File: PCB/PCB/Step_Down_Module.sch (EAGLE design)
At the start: 22 parts, among them Q1 TPH2900ENH

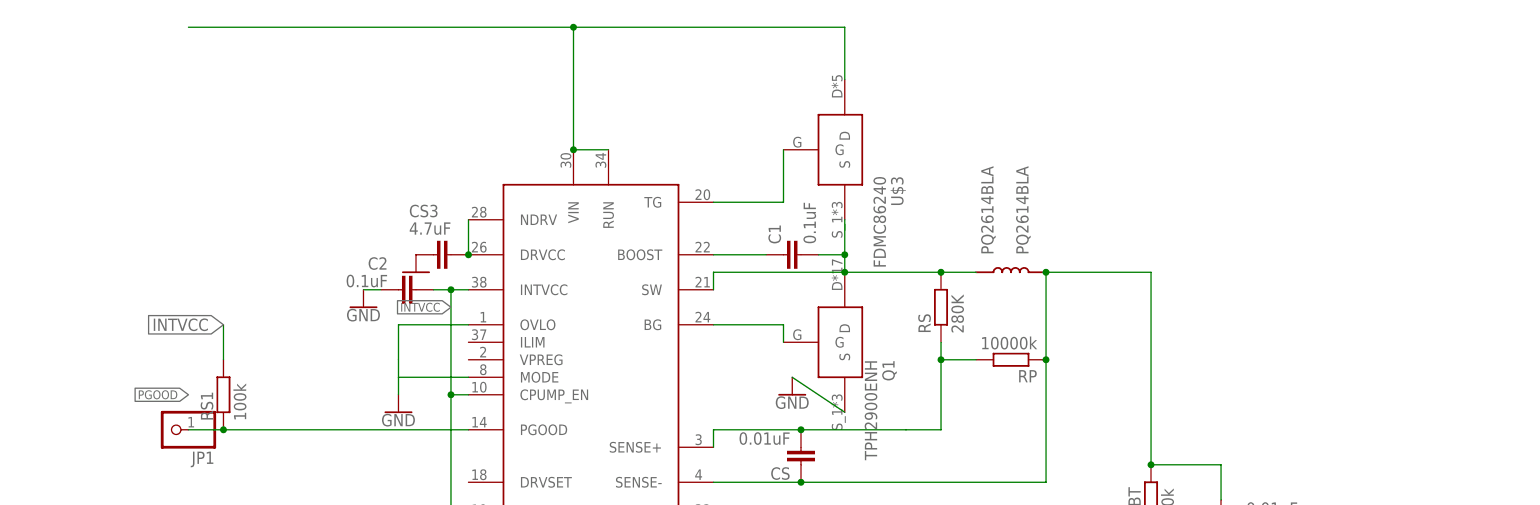
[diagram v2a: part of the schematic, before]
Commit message: Working on schematic - Added I/O capacitors
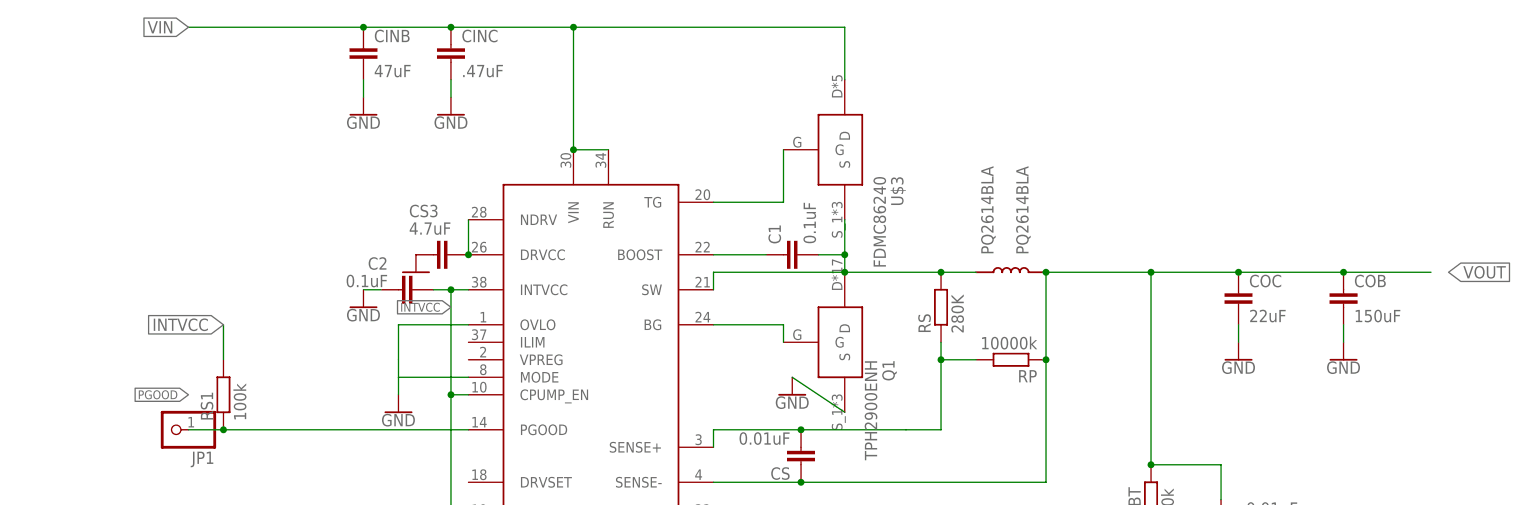
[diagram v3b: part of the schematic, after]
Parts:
- added CINB: 47uF, rcl:C-EUC0805
- added CINC: .47uF, rcl:C-EUC0805
- added COB: 150uF, rcl:C-EUC0805
- added COC: 22uF, rcl:C-EUC0805
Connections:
- removed net N$5: CS.1, CS1.2, RFBT.2, RP.1, U$1.SENSE-, U$2.P$2
- removed net N$9: U$1.RUN, U$1.VIN, U$3.D
- new net VIN: CINB.1, CINC.1, U$1.RUN, U$1.VIN, U$3.D
- new net VOUT: COB.1, COC.1, CS.1, CS1.2, RFBT.2, RP.1, U$1.SENSE-, U$2.P$2
- net GND: now also CINB.2, CINC.2, COB.2, COC.2
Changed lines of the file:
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@@
 <part name="CS3" library="rcl" library_urn="urn:adsk.eagle:library:334" deviceset="C-EU" device="C0805" package3d_urn="urn:adsk.eagle:package:23617/2" value="4.7uF"/>
 <part name="GND10" library="SparkFun-PowerSymbols" library_urn="urn:adsk.eagle:library:530" deviceset="GND" device=""/>
+<part name="CINB" library="rcl" library_urn="urn:adsk.eagle:library:334" deviceset="C-EU" device="C0805" package3d_urn="urn:adsk.eagle:package:23617/2" value="47uF"/>
+<part name="CINC" library="rcl" library_urn="urn:adsk.eagle:library:334" deviceset="C-EU" device="C0805" package3d_urn="urn:adsk.eagle:package:23617/2" value=".47uF"/>
+<part name="COC" library="rcl" library_urn="urn:adsk.eagle:library:334" deviceset="C-EU" device="C0805" package3d_urn="urn:adsk.eagle:package:23617/2" value="22uF"/>
+<part name="COB" library="rcl" library_urn="urn:adsk.eagle:library:334" deviceset="C-EU" device="C0805" package3d_urn="urn:adsk.eagle:package:23617/2" value="150uF"/>
+<part name="GND11" library="SparkFun-PowerSymbols" library_urn="urn:adsk.eagle:library:530" deviceset="GND" device=""/>
+<part name="GND12" library="SparkFun-PowerSymbols" library_urn="urn:adsk.eagle:library:530" deviceset="GND" device=""/>
+<part name="GND13" library="SparkFun-PowerSymbols" library_urn="urn:adsk.eagle:library:530" deviceset="GND" device=""/>
+<part name="GND14" library="SparkFun-PowerSymbols" library_urn="urn:adsk.eagle:library:530" deviceset="GND" device=""/>
 </parts>
 <sheets>
@@
 </instance>
 <instance part="GND10" gate="1" x="-5.08" y="73.66" smashed="yes"/>
+<instance part="CINB" gate="G$1" x="-12.7" y="106.68"/>
+<instance part="CINC" gate="G$1" x="0" y="106.68"/>
+<instance part="COC" gate="G$1" x="114.3" y="71.12"/>
+<instance part="COB" gate="G$1" x="129.54" y="71.12"/>
+<instance part="GND11" gate="1" x="114.3" y="60.96"/>
+<instance part="GND12" gate="1" x="129.54" y="60.96"/>
+<instance part="GND13" gate="1" x="-12.7" y="96.52"/>
+<instance part="GND14" gate="1" x="0" y="96.52"/>
 </instances>
 <busses>
@@
 </segment>
 </net>
-<net name="N$5" class="0">
+<net name="VOUT" class="0">
 <segment>
 <pinref part="U$2" gate="G$1" pin="P$2"/>
@@
 <wire x1="111.76" y1="45.72" x2="111.76" y2="40.64" width="0.1524" layer="91"/>
 <junction x="101.6" y="45.72"/>
+<pinref part="COC" gate="G$1" pin="1"/>
+<wire x1="114.3" y1="73.66" x2="101.6" y2="73.66" width="0.1524" layer="91"/>
+<junction x="101.6" y="73.66"/>
+<pinref part="COB" gate="G$1" pin="1"/>
+<wire x1="129.54" y1="73.66" x2="114.3" y2="73.66" width="0.1524" layer="91"/>
+<junction x="114.3" y="73.66"/>
+<wire x1="129.54" y1="73.66" x2="142.24" y2="73.66" width="0.1524" layer="91"/>
+<junction x="129.54" y="73.66"/>
+<label x="144.78" y="73.66" size="1.778" layer="95" xref="yes"/>
 </segment>
 </net>
@@
 </segment>
 </net>
-<net name="N$9" class="0">
+<net name="VIN" class="0">
 <segment>
 <pinref part="U$1" gate="G$1" pin="VIN"/>
@@
 <wire x1="17.78" y1="91.44" x2="22.86" y2="91.44" width="0.1524" layer="91"/>
 <wire x1="17.78" y1="91.44" x2="17.78" y2="109.22" width="0.1524" layer="91"/>
-<wire x1="17.78" y1="109.22" x2="-38.1" y2="109.22" width="0.1524" layer="91"/>
+<wire x1="17.78" y1="109.22" x2="0" y2="109.22" width="0.1524" layer="91"/>
 <junction x="17.78" y="91.44"/>
 <pinref part="U$3" gate="G$1" pin="D"/>
+<wire x1="0" y1="109.22" x2="-12.7" y2="109.22" width="0.1524" layer="91"/>
+<wire x1="-12.7" y1="109.22" x2="-38.1" y2="109.22" width="0.1524" layer="91"/>
 <wire x1="57.15" y1="101.6" x2="57.15" y2="109.22" width="0.1524" layer="91"/>
 <wire x1="57.15" y1="109.22" x2="17.78" y2="109.22" width="0.1524" layer="91"/>
 <junction x="17.78" y="109.22"/>
+<pinref part="CINB" gate="G$1" pin="1"/>
+<junction x="-12.7" y="109.22"/>
+<pinref part="CINC" gate="G$1" pin="1"/>
+<junction x="0" y="109.22"/>
+<label x="-38.1" y="109.22" size="1.778" layer="95" rot="R180" xref="yes"/>
 </segment>
 </net>
@@
 <pinref part="GND10" gate="1" pin="GND"/>
 </segment>
-</net>
+<segment>
+<pinref part="GND13" gate="1" pin="GND"/>
+<pinref part="CINB" gate="G$1" pin="2"/>
+<wire x1="-12.7" y1="99.06" x2="-12.7" y2="101.6" width="0.1524" layer="91"/>
+</segment>
+<segment>
+<pinref part="GND14" gate="1" pin="GND"/>
+<pinref part="CINC" gate="G$1" pin="2"/>
+<wire x1="0" y1="99.06" x2="0" y2="101.6" width="0.1524" layer="91"/>
+</segment>
+<segment>
+<pinref part="GND11" gate="1" pin="GND"/>
+<pinref part="COC" gate="G$1" pin="2"/>
+<wire x1="114.3" y1="63.5" x2="114.3" y2="66.04" width="0.1524" layer="91"/>
+</segment>
+<segment>
+<pinref part="GND12" gate="1" pin="GND"/>
+<pinref part="COB" gate="G$1" pin="2"/>
+<wire x1="129.54" y1="63.5" x2="129.54" y2="66.04" width="0.1524" layer="91"/>
+</segment>
+</net>

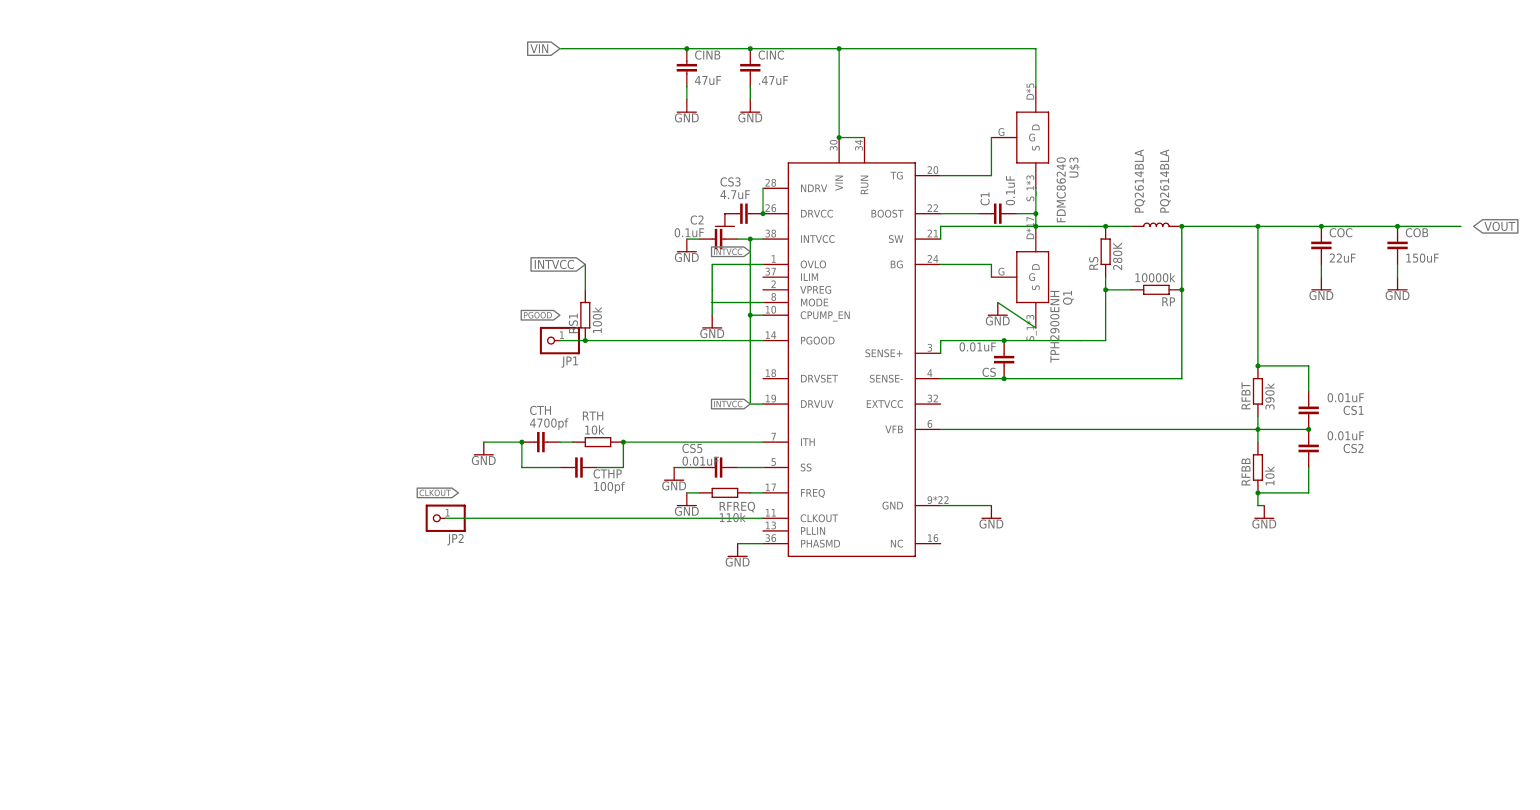
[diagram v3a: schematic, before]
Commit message: Working on schematic - Added DRVCC transistor, made a lot of changes to the pin state
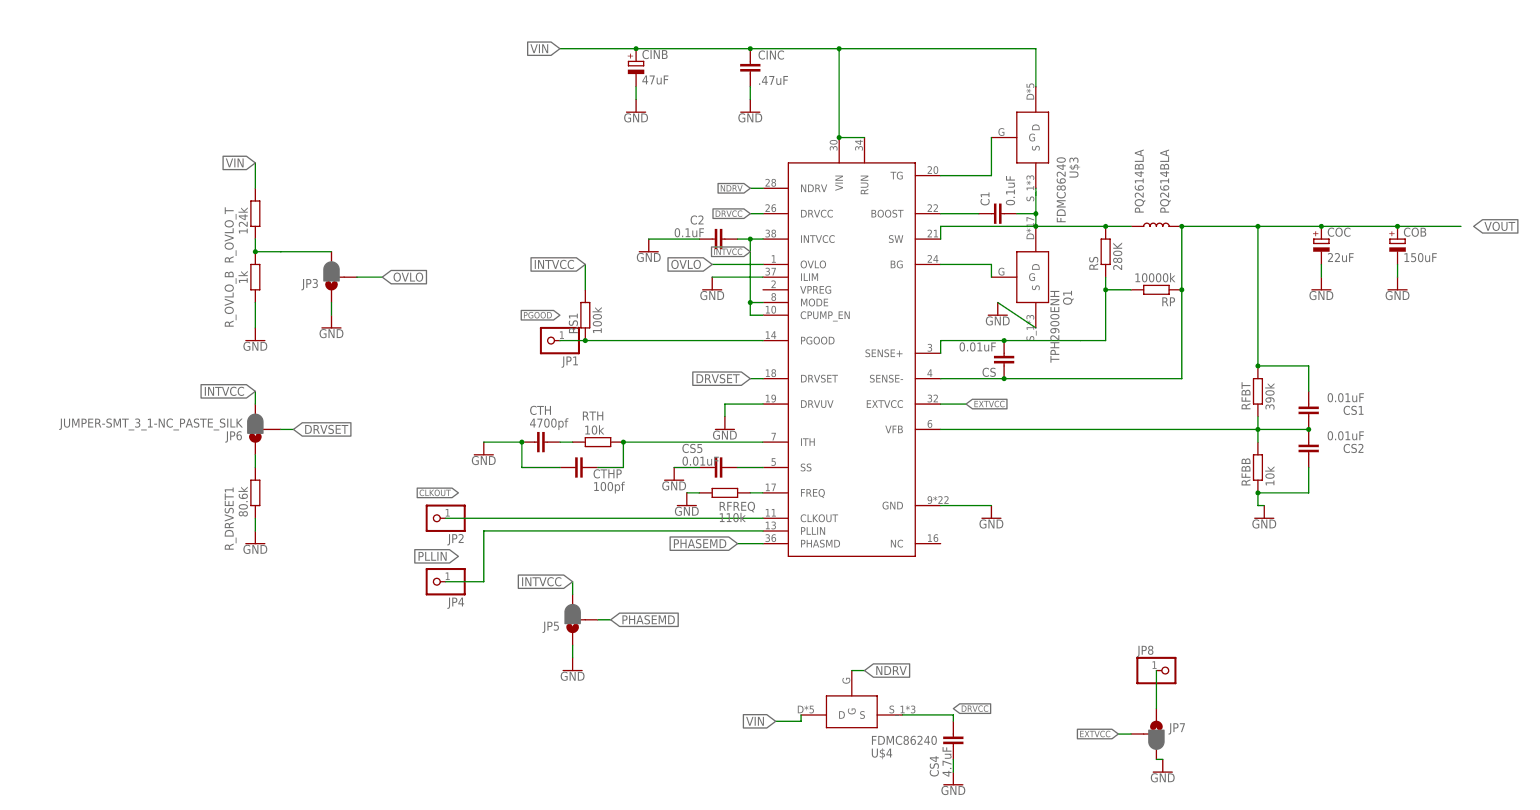
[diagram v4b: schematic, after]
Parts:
- removed CS3: 4.7uF, rcl:C-EUC0805
- added CS4: 4.7uF, rcl:C-EUC0805
- added JP3, JP5, JP6, JP7: JUMPER-SMT_3_1-NC_PASTE_SILK, SparkFun-Jumpers:JUMPER-SMT_3_1-NC_PASTE_SILK
- added JP4, JP8: (no value), pinhead:PINHD-1X1
- added R_DRVSET1: 80.6k, rcl:R-EU_R0805
- added R_OVLO_B: 1k, rcl:R-EU_R0805
- added R_OVLO_T: 124k, rcl:R-EU_R0805
- added U$4: FDMC86240, Switching_MOS:FDMC86240
- CINB: device rcl:C-EUC0805 -> rcl:CPOL-EUE7.5-16
- CINC: device rcl:C-EUC0805 -> rcl:C-EU150-084X183
- COB: device rcl:C-EUC0805 -> rcl:CPOL-EUE5-10.5
- COC: device rcl:C-EUC0805 -> rcl:CPOL-EUE5-5
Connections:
- removed net N$14: CS3.1, U$1.DRVCC, U$1.NDRV
- new net DRVCC: CS4.1, U$1.DRVCC, U$4.S
- new net DRVSET: JP6.2, U$1.DRVSET
- new net EXTVCC: JP7.2, U$1.EXTVCC
- new net N$13: JP7.1, JP8.1
- new net N$5: JP6.1, R_DRVSET1.1
- new net N$9: JP3.3, R_OVLO_B.1, R_OVLO_T.2
- new net NDRV: U$1.NDRV, U$4.G
- new net OVLO: JP3.2, U$1.OVLO
- new net PHASEMD: JP5.2, U$1.PHASMD
- new net PLLIN: JP4.1, U$1.PLLIN
- net GND: now also CINB.-, COB.-, COC.-, CS4.2, JP3.1, JP5.1, JP7.3, R_DRVSET1.2, R_OVLO_B.2, U$1.DRVUV, U$1.ILIM; no longer CINB.2, COB.2, COC.2, CS3.2, U$1.MODE, U$1.OVLO, U$1.PHASMD
- net INTVCC: now also JP5.3, JP6.3, U$1.MODE; no longer U$1.DRVUV
- net VIN: now also CINB.+, R_OVLO_T.1, U$4.D; no longer CINB.1
- net VOUT: now also COB.+, COC.+; no longer COB.1, COC.1

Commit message: Removed folder: Adithya
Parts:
- removed C1: 0.1uF, rcl:C-EUC0805
- added CINC1: .47uF, rcl:C-EU150-084X183
- added COB1: 150uF, rcl:CPOL-EUE5-10.5
- added COC1: 22uF, rcl:CPOL-EUE5-5
- added POT_FB: 10k, rcl:R-TRIMM64W
- added RS2: 10k, rcl:R-EU_R0805
- RFBB: value 10k -> 4.7k
- RFBT: value 390k -> 180k
- RS: value 280K -> 270k
- R_OVLO_T: value 124k -> 120k
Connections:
- net N$10 renamed ITH
- net N$7 renamed SS
- new net N$14: CS1.2, POT_FB.S, RFBT.2
- new net N$7: RS.1, RS2.2
- net GND: now also COB1.-, COC1.-, POT_FB.E
- net N$3: now also CINC1.2; no longer C1.2
- net N$4: now also CINC1.1; no longer C1.1
- net N$6: now also RS2.1; no longer RS.1
- net VOUT: now also COB1.+, COC1.+, POT_FB.A; no longer CS1.2, RFBT.2
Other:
- moved on the sheet: RP

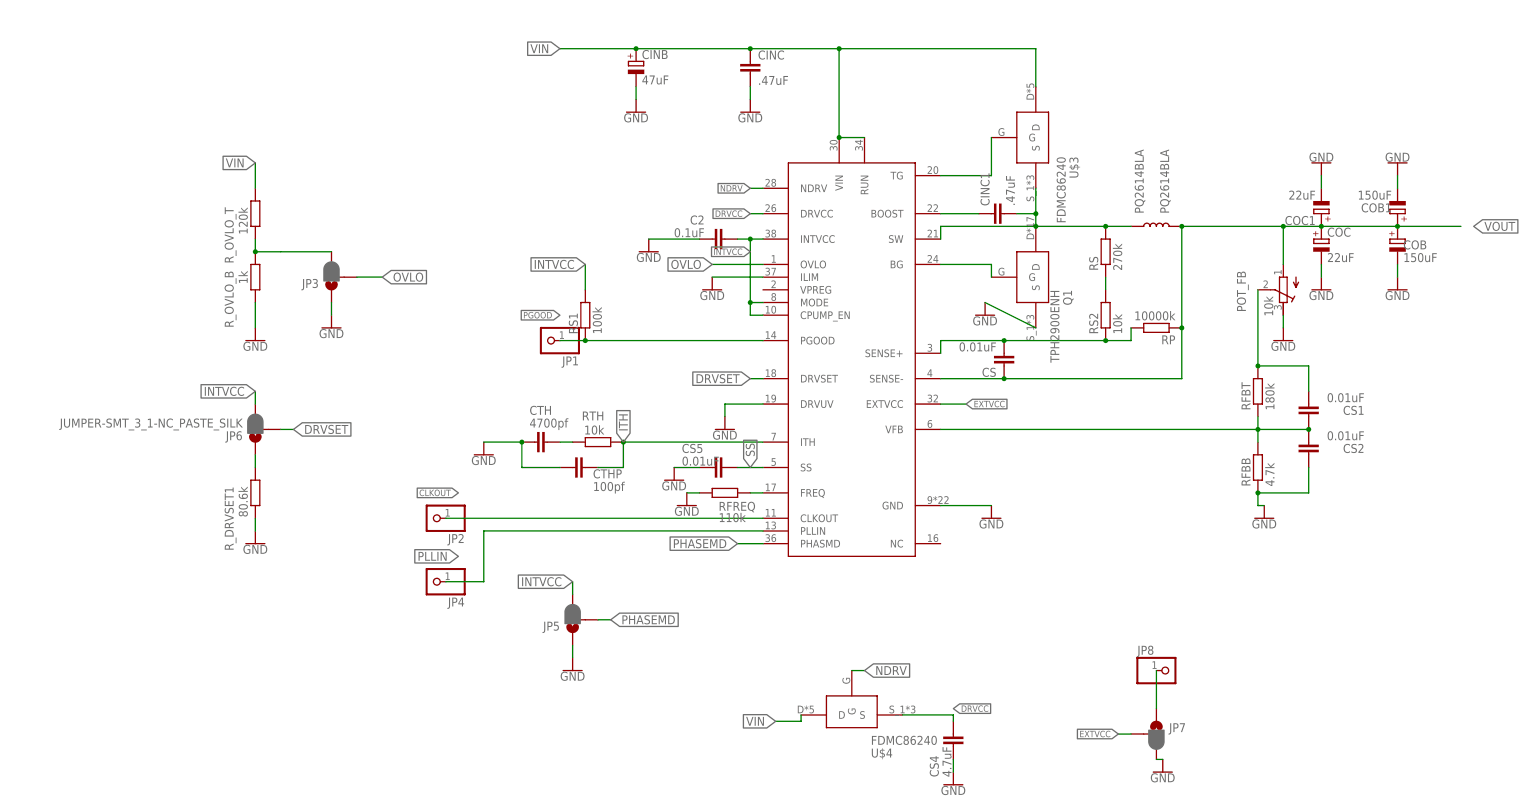
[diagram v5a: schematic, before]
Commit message: Initial routing of PCB with design considerations
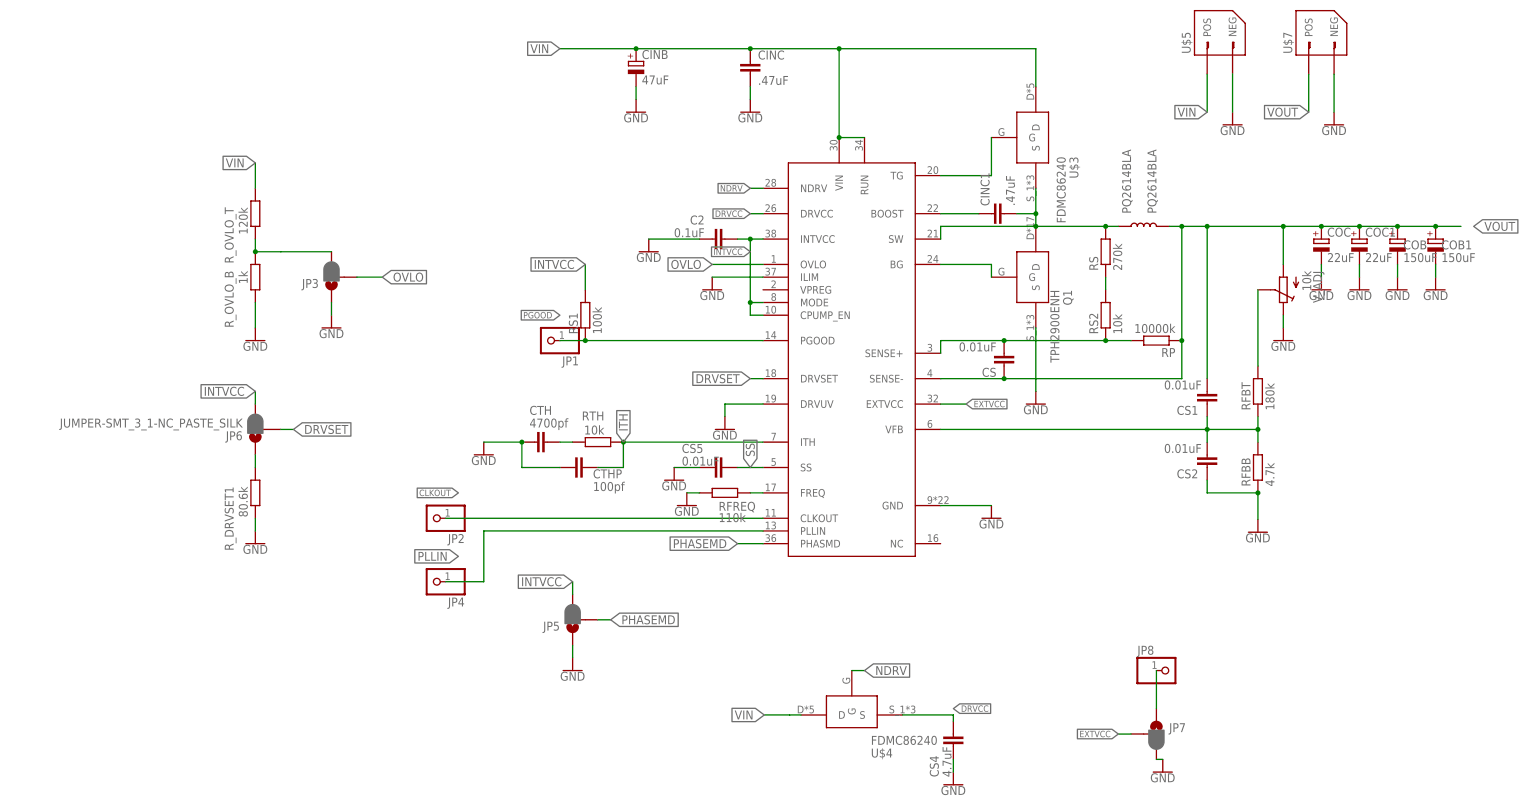
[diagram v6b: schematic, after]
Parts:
- removed POT_FB: 10k, rcl:R-TRIMM64W
- removed U$2: PQ2614BLA, Inductors:PQ2614BLA
- added L1: PQ2614BLA, Inductors:PQ2614BLA
- added U$5, U$7: IO_PAD, IO_pad:IO_PAD
- added V_ADJ: 10k, pot:RM065
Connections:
- net GND: now also U$5.NEG, U$7.NEG, V_ADJ.E; no longer POT_FB.E
- net N$14: now also V_ADJ.S; no longer CS1.2, POT_FB.S
- net N$3: now also L1.P$1; no longer U$2.P$1
- net VIN: now also U$5.POS
- net VOUT: now also CS1.2, L1.P$2, U$7.POS, V_ADJ.A; no longer POT_FB.A, U$2.P$2
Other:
- moved on the sheet: COB1, COC1, CS1, CS2, RP
